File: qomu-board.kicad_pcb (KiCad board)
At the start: 4 copper layers, 33.3 x 12.2 mm, 71 parts, among them IC1 EOS-S3, J1 FTSH-105-01-L-DV-K, J2 825437-4, J3 MC-HVT1-S02-G, J4 USB-C, Q1 RV1C002UN, Q2 RV1C002UN, Q3 RV1C002UN, SW2 Captouch Pads, U1 MIC5504-3.3YMT, U10 UHD1110-FKA, U2 MIC5504-3.3YMT, U4 GD25Q16CEIGR, U9 USB-B

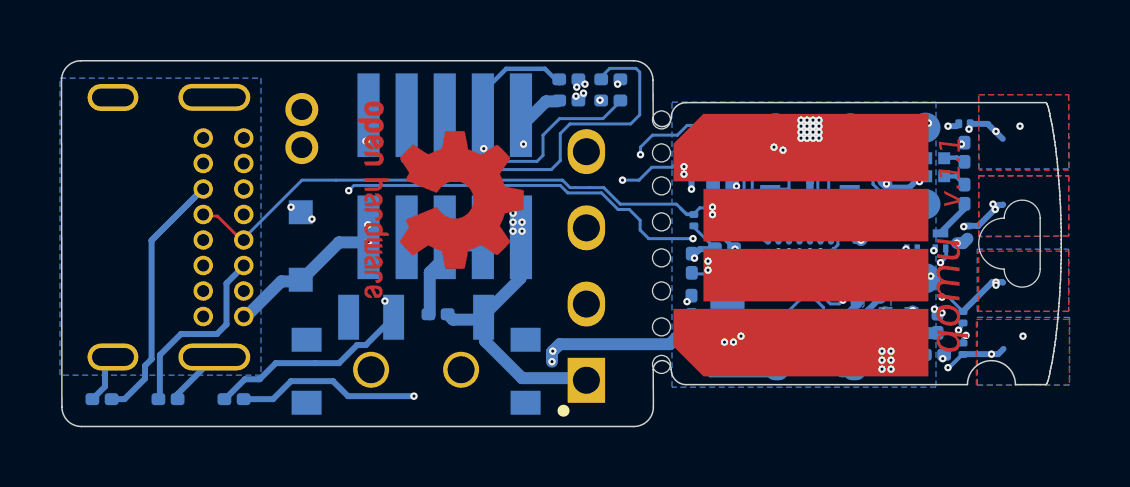
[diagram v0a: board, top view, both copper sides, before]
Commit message: pcb: fix phantom In.Cu4 vias
There were two vias that were still going to In.Cu4 despite this layer
no longer existing.

Signed-off-by: Sean Cross <sean@xobs.io>
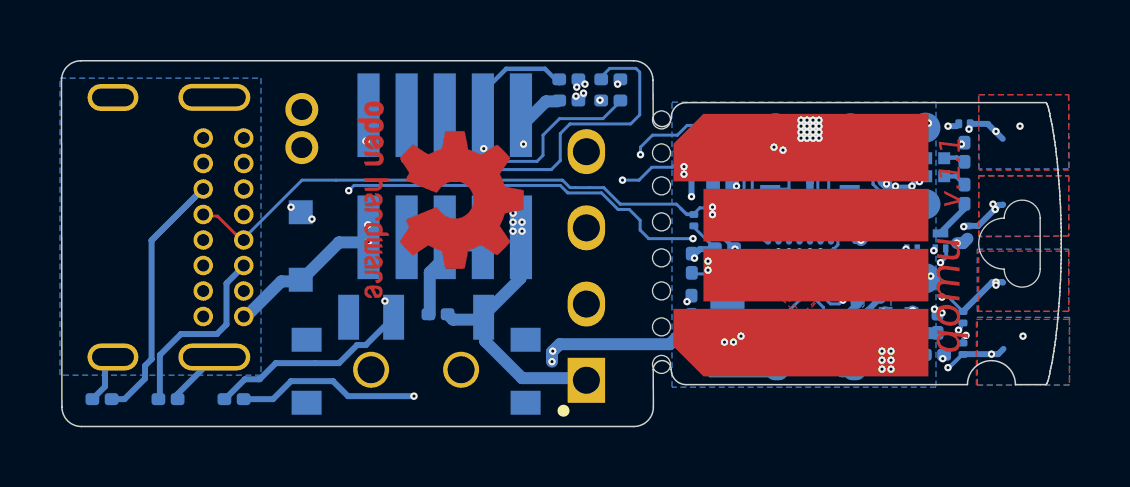
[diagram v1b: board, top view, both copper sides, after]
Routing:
- net +3V3: track 85.5 -> 80.4 mm, vias 40 -> 42
- net /RST_N: track 35.8 -> 36.7 mm
- added copper zone on F.Cu, net +3V3

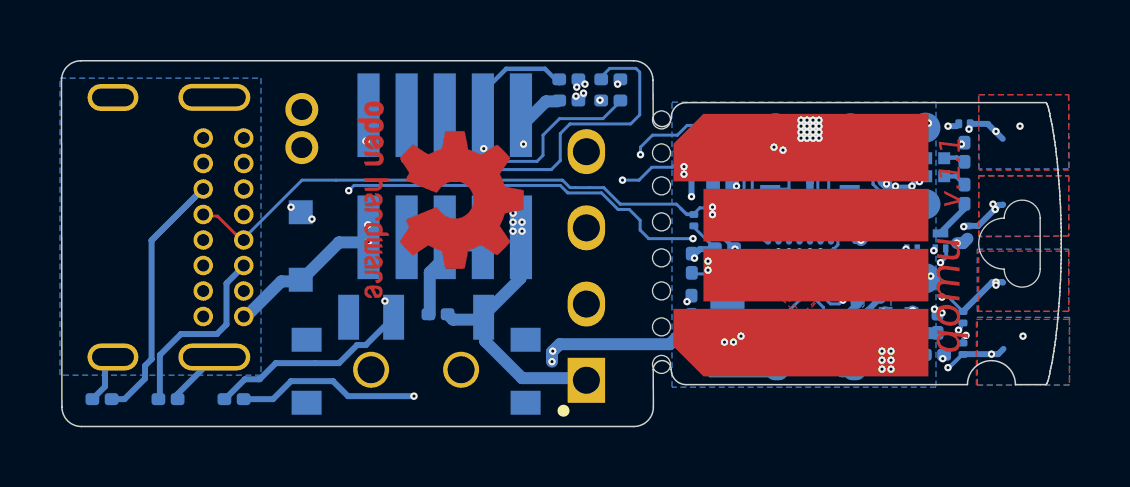
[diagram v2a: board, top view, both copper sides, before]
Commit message: pcb: lay out new SWD pads
Signed-off-by: Sean Cross <sean@xobs.io>
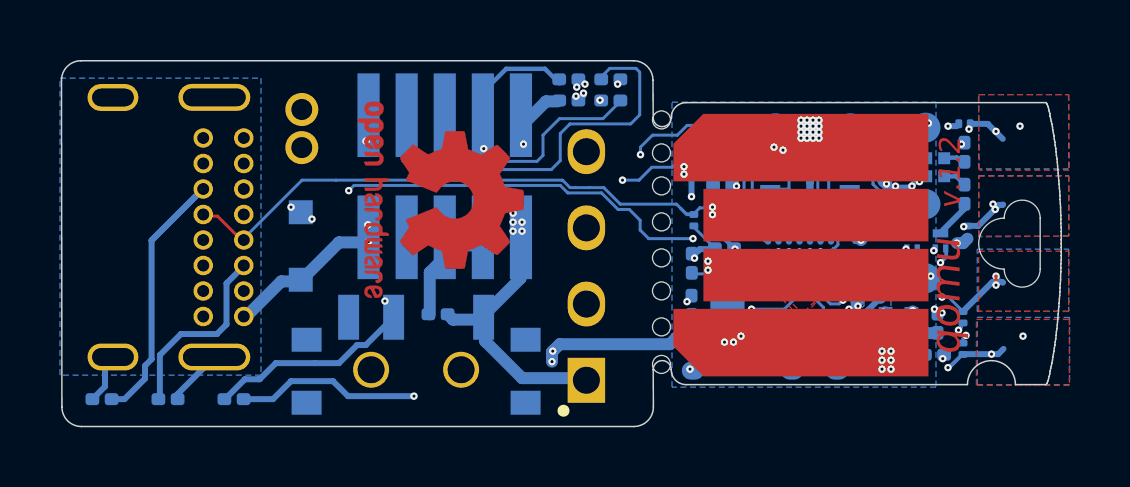
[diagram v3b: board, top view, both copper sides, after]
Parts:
- removed TP9: TP_SMD_0_75MM, qomu-board-footprints:Testpoint_smd_0_75_0_6mm
- added TP2: TP_SMD_0_75MM, qomu-board-footprints:Testpoint_smd_0_75_0_6mm, B.Cu at (38.3, 27.0)
- added TP8: TP_SMD_0_75MM, qomu-board-footprints:Testpoint_smd_0_75_0_6mm, B.Cu at (33.5, 27.0)
- R10, R7: value 0R, 0201 -> DNP, 0R, 0201
- moved TP3 0.50 mm to (36.8, 27.0)
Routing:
- net GND: track 148.4 -> 157.9 mm, vias 80 -> 82
- net /SWD_IO: track 17.6 -> 22.5 mm, vias 2 -> 3
- net /C1: track 30.2 -> 31.5 mm
- net /TOUCH_2: track 11.9 -> 13.0 mm
- net +3V3: track 80.4 -> 81.4 mm
- net +VBUS: track 53.8 -> 53.0 mm
- net /SWD_CLK: track 22.6 -> 21.9 mm, vias 2 -> 3
- added copper zone on In2.Cu, net +VBUS
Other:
- board text added: "v.1.2"
- board text removed: "v.1.1"

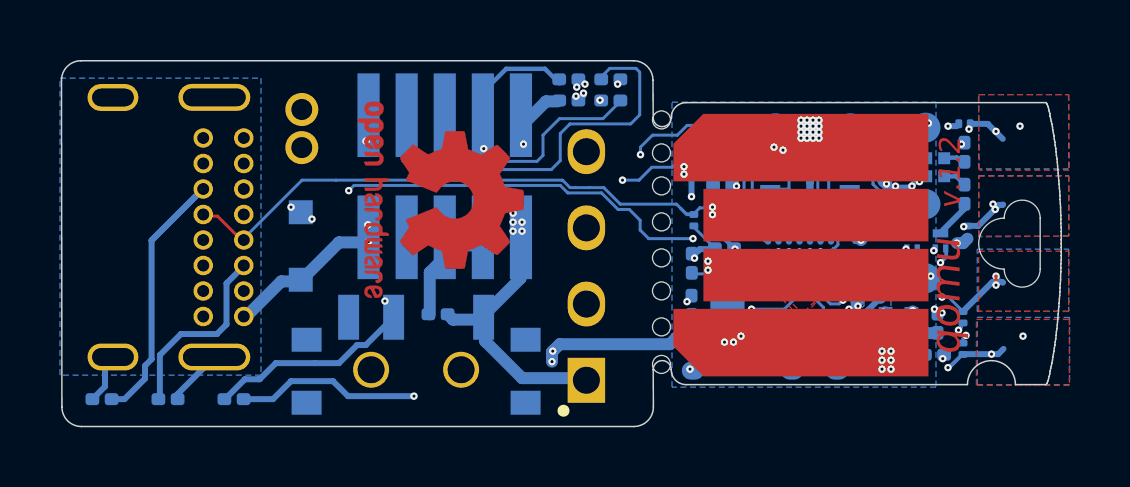
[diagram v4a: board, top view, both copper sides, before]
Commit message: pcb: fix silkscreen layers
Some components were showing on the silkscreen layer, which wasn't what
we wanted. This caused overlapping of pads.

Disable the reference designator on those pards.

Signed-off-by: Sean Cross <sean@xobs.io>
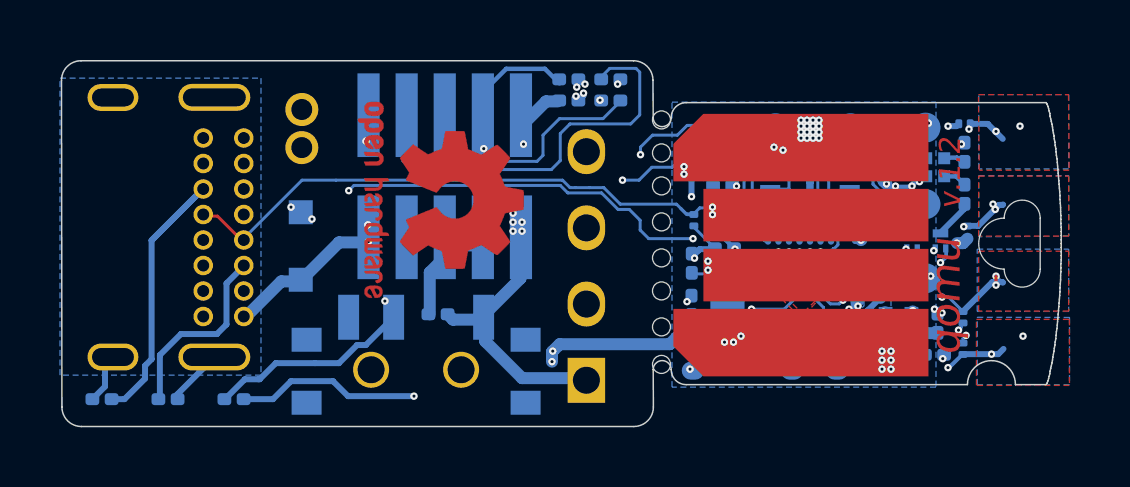
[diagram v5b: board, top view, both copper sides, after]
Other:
- board text added: "IO"
- board text added: "K"
- board text removed: "E"

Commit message: pcb: move VUSB trace to "front" side
By moving this trace to the font side, we allow the ground plane on the
back side to continue uninterrupted.

Signed-off-by: Sean Cross <sean@xobs.io>
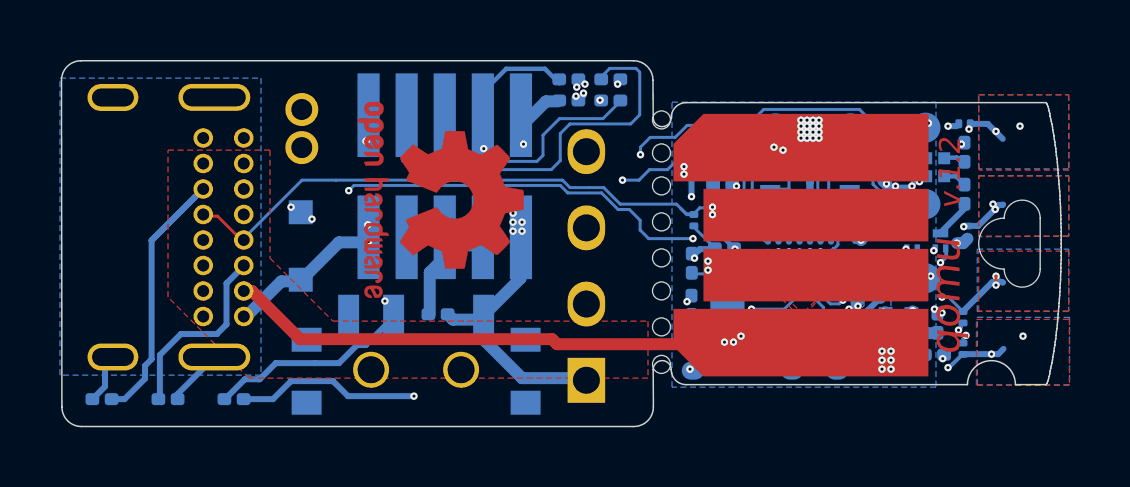
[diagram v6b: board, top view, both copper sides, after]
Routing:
- net GND: track 157.9 -> 167.2 mm, vias 82 -> 83
- net +3V3: track 81.4 -> 85.9 mm
- net +VBUS: track 53.0 -> 55.2 mm, vias 24 -> 20
- net /C1: track 31.5 -> 30.8 mm
- added copper zone on F.Cu, net +VBUS

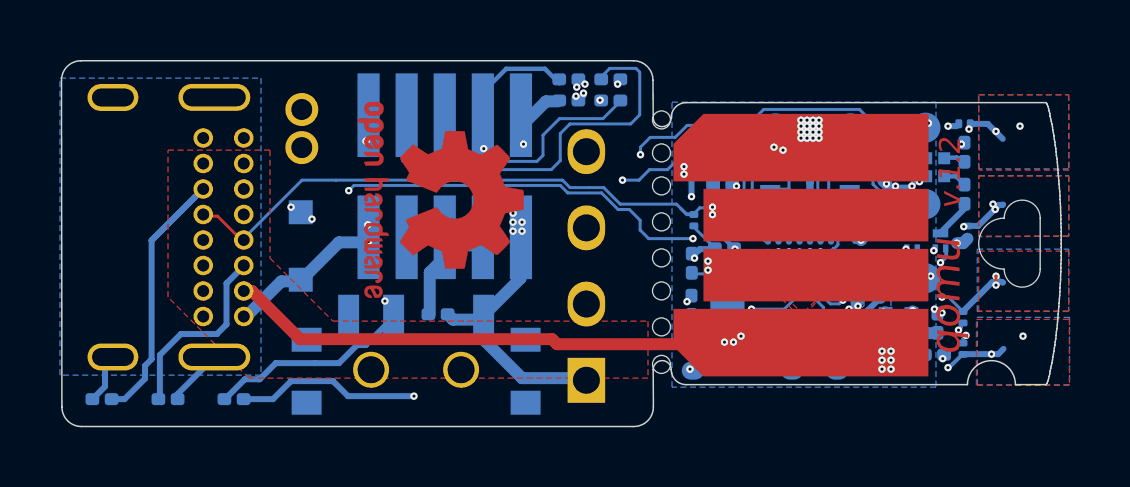
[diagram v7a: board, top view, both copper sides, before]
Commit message: pcb: gnd: increase via spacing due to DRC check
The PCB house said the GND vias were too close. Move them further apart
to prevent design issues.

Signed-off-by: Sean Cross <sean@xobs.io>
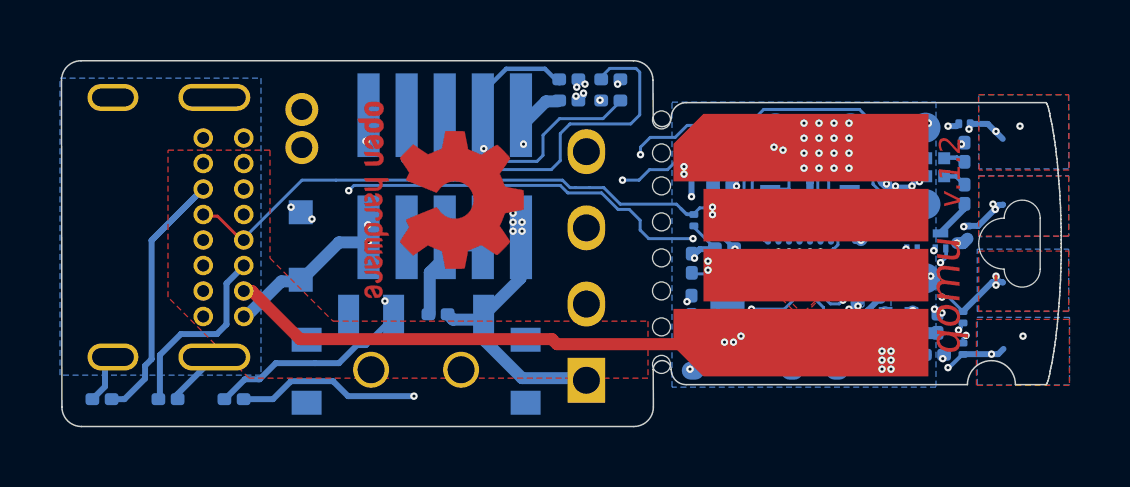
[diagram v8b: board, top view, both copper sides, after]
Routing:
- net GND: track 167.2 -> 160.8 mm
